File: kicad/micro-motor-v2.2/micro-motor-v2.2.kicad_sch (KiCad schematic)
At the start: 29 parts, among them J101 SUPPLY, J103 Hall, J104 Encoder, J106 Motor, J201 CAN

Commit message: ready to order
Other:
- title: Micro-Motor V2.1 -> Micro-Motor V2.2
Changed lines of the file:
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@@
   (paper "A4")
   (title_block
-    (title "Micro-Motor V2.1")
-    (date "2021-07-31")
+    (title "Micro-Motor V2.2")
+    (date "2023-07-25")
     (rev "1")
     (company "Roboterclub Aachen e.V.")

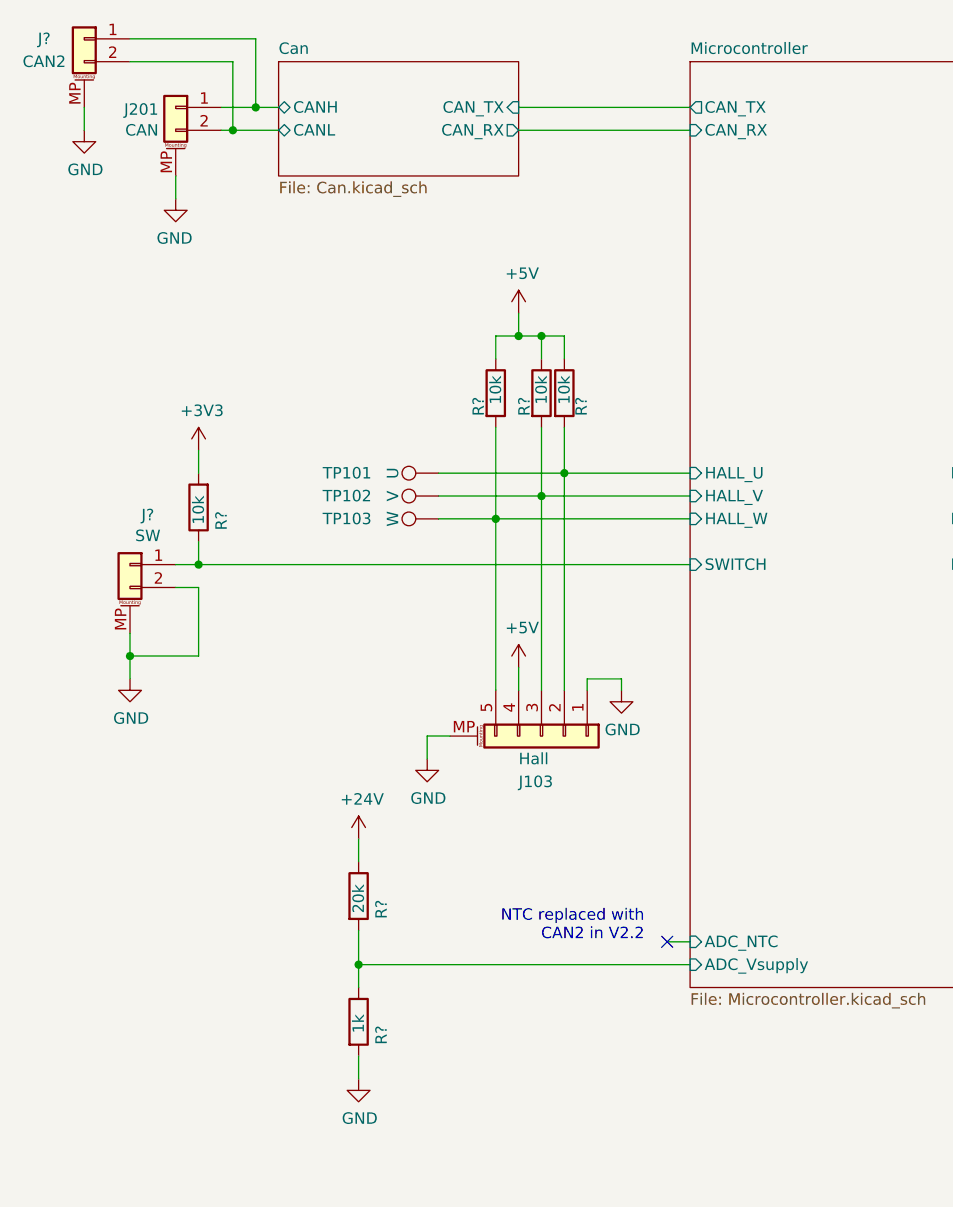
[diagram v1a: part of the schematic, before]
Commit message: [CI] Attempt to fix ERC
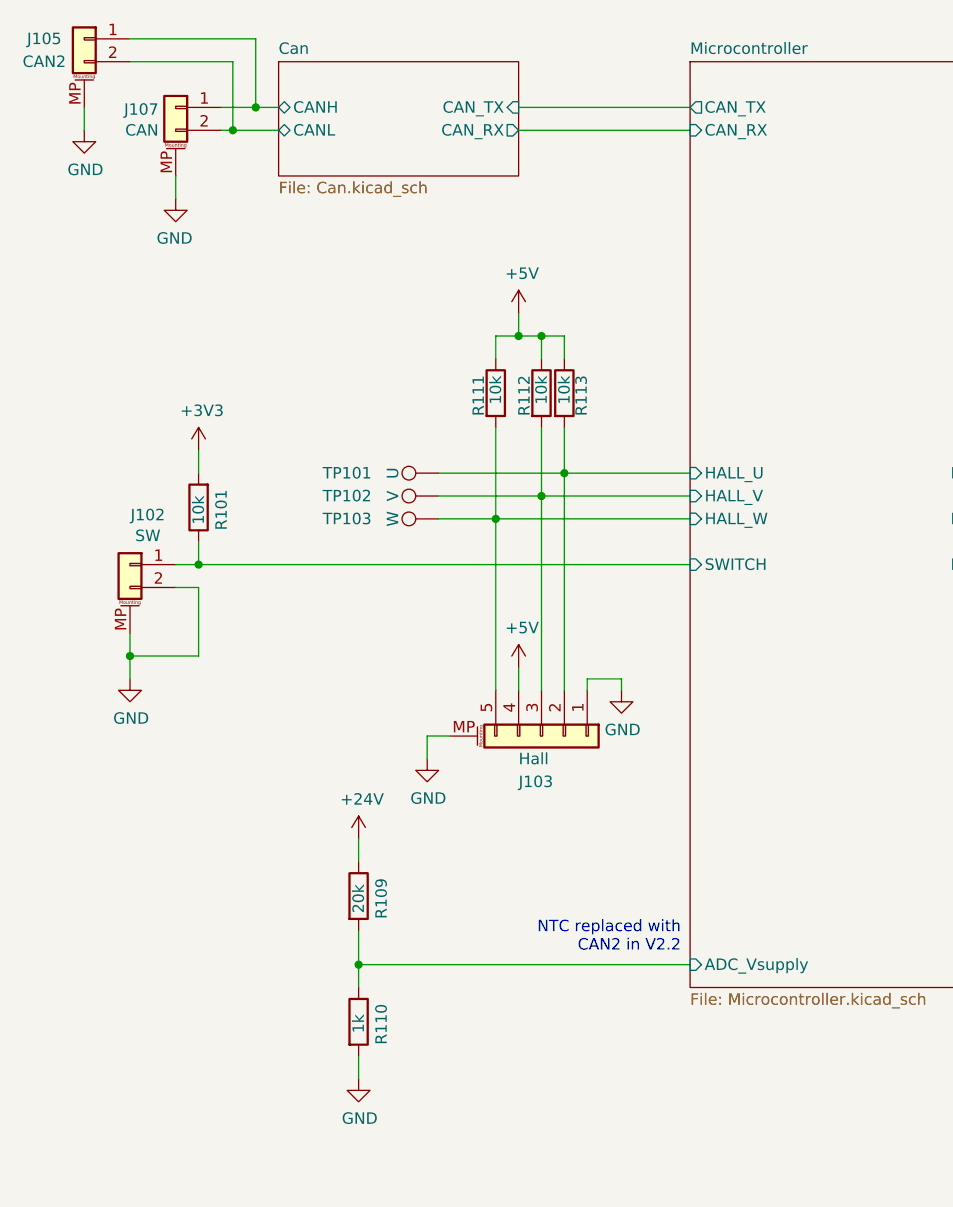
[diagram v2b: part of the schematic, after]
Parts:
- gave numbers to parts that had none: 8
- renumbered J201 to J107
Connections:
- no-connect marks 1 -> 0
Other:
- sheet Microcontroller ports: added none; removed ADC_NTC
